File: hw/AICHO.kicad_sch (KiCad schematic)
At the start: 73 parts, among them J1 Conn_01x06, J101 Conn_01x03, J102 Conn_01x02, J103 Conn_01x02, J104 Conn_01x02, J2 Conn_01x02, J201 Conn_01x03, J202 Conn_01x02, J203 Conn_01x02, J204 Conn_01x02, J3 USB_A, J301 Conn_01x03, J302 Conn_01x02, J303 Conn_01x02, J304 Conn_01x02, J4 AudioJack3_SwitchTR, J401 Conn_01x03, J402 Conn_01x02, J403 Conn_01x02, J404 Conn_01x02, J5 Speaker, Q1 Si2302, Q10 Si2302, Q11 Si2302, Q12 Si2302, Q2 Si2302, Q3 Si2302, Q4 Si2302, Q5 Si2302, Q6 Si2302, Q7 Si2302, Q8 Si2302, Q9 Si2302, U1 RP2040, U2 W25Q128JVPIQ, U3 SPX3819M5-L-3-3, U4 USBLC6-2SC6, U5 MAX98357AETE+, Y1 12MHz

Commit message: More routing (is this perfectionism??)
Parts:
- added C17: 100n, Capacitor_SMD:C_0402_1005Metric, symbol Device:C
- added J22: Conn_01x02, Connector_PinHeader_2.54mm:PinHeader_1x02_P2.54mm_Vertical, symbol Connector_Generic:Conn_01x02
- renumbered C17 to C18, C18 to C19, J2 to J21
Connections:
- net +5V: now also C17.1, J22.1 (Pin_1)
- net GND: now also C17.2, J22.2 (Pin_2)
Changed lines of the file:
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@@
   (junction (at 159.385 29.845) (diameter 0) (color 0 0 0 0)
   )
+  (junction (at 252.095 34.29) (diameter 0) (color 0 0 0 0)
+  )
   (junction (at 31.115 26.035) (diameter 0) (color 0 0 0 0)
   )
@@
     (stroke (width 0) (type default))
   )
+  (wire (pts (xy 47.625 26.035) (xy 45.72 26.035))
+    (stroke (width 0) (type default))
+  )
   (wire (pts (xy 262.89 140.97) (xy 264.795 140.97))
     (stroke (width 0) (type default))
@@
     (stroke (width 0) (type default))
   )
+  (wire (pts (xy 47.625 28.575) (xy 45.72 28.575))
+    (stroke (width 0) (type default))
+  )
   (wire (pts (xy 142.24 207.01) (xy 143.51 207.01))
     (stroke (width 0) (type default))
@@
     (stroke (width 0) (type default))
   )
+  (wire (pts (xy 252.095 34.29) (xy 252.095 43.18))
+    (stroke (width 0) (type default))
+  )
   (wire (pts (xy 158.115 81.28) (xy 156.21 81.28))
     (stroke (width 0) (type default))
@@
     (stroke (width 0) (type default))
   )
+  (wire (pts (xy 252.095 34.29) (xy 258.445 34.29))
+    (stroke (width 0) (type default))
+  )
   (wire (pts (xy 101.6 154.94) (xy 102.87 154.94))
     (stroke (width 0) (type default))
@@
   (symbol (lib_id "Connector_Generic:Conn_01x02") (at 24.13 26.035 0) (mirror y) (unit 1)
     (in_bom yes) (on_board yes) (dnp no)
-    (property "Reference" "J2" (at 24.13 22.86 0)
+    (property "Reference" "J21" (at 24.13 22.86 0)
       (effects (font (size 1.27 1.27)))
     )
@@
       (project "AICHO"
         (path "/1352642d-7cf1-4ee5-b8a3-66f2011ace6c"
-          (reference "J2") (unit 1)
+          (reference "J21") (unit 1)
         )
       )
@@
     )
   )
+  (symbol (lib_id "power:GND") (at 258.445 41.91 0) (mirror y) (unit 1)
+    (in_bom yes) (on_board yes) (dnp no)
+    (property "Reference" "#PWR069" (at 258.445 48.26 0)
+      (effects (font (size 1.27 1.27)) hide)
+    )
+    (property "Value" "GND" (at 258.445 46.355 0)
+      (effects (font (size 1.27 1.27)) hide)
+    )
+    (property "Footprint" "" (at 258.445 41.91 0)
+      (effects (font (size 1.27 1.27)) hide)
+    )
+    (property "Datasheet" "" (at 258.445 41.91 0)
+      (effects (font (size 1.27 1.27)) hide)
+    )
+    (pin "1")
+    (instances
+      (project "AICHO"
+        (path "/1352642d-7cf1-4ee5-b8a3-66f2011ace6c"
+          (reference "#PWR069") (unit 1)
+        )
+      )
+    )
+  )
   (symbol (lib_id "power:+5V") (at 151.13 197.485 0) (unit 1)
     (in_bom yes) (on_board yes) (dnp no) (fields_autoplaced)
@@
     )
   )
+  (symbol (lib_id "Connector_Generic:Conn_01x02") (at 40.64 26.035 0) (mirror y) (unit 1)
+    (in_bom yes) (on_board yes) (dnp no)
+    (property "Reference" "J22" (at 40.64 22.86 0)
+      (effects (font (size 1.27 1.27)))
+    )
+    (property "Value" "Conn_01x02" (at 40.64 22.86 0)
+      (effects (font (size 1.27 1.27)) hide)
+    )
+    (property "Footprint" "Connector_PinHeader_2.54mm:PinHeader_1x02_P2.54mm_Vertical" (at 40.64 26.035 0)
+      (effects (font (size 1.27 1.27)) hide)
+    )
+    (property "Datasheet" "~" (at 40.64 26.035 0)
+      (effects (font (size 1.27 1.27)) hide)
+    )
+    (pin "2")
+    (pin "1")
+    (instances
+      (project "AICHO"
+        (path "/1352642d-7cf1-4ee5-b8a3-66f2011ace6c"
+          (reference "J22") (unit 1)
+        )
+      )
+    )
+  )
   (symbol (lib_id "Regulator_Linear:SPX3819M5-L-3-3") (at 38.1 44.45 0) (unit 1)
     (in_bom yes) (on_board yes) (dnp no) (fields_autoplaced)
@@
     )
   )
-  (symbol (lib_id "power:+5V") (at 252.095 43.18 0) (unit 1)
+  (symbol (lib_id "power:+5V") (at 252.095 34.29 0) (unit 1)
     (in_bom yes) (on_board yes) (dnp no) (fields_autoplaced)
-    (property "Reference" "#PWR024" (at 252.095 46.99 0)
+    (property "Reference" "#PWR024" (at 252.095 38.1 0)
       (effects (font (size 1.27 1.27)) hide)
     )
-    (property "Value" "+5V" (at 252.095 38.735 0)
+    (property "Value" "+5V" (at 252.095 29.845 0)
       (effects (font (size 1.27 1.27)))
     )
-    (property "Footprint" "" (at 252.095 43.18 0)
+    (property "Footprint" "" (at 252.095 34.29 0)
       (effects (font (size 1.27 1.27)) hide)
     )
-    (property "Datasheet" "" (at 252.095 43.18 0)
+    (property "Datasheet" "" (at 252.095 34.29 0)
       (effects (font (size 1.27 1.27)) hide)
     )
@@
   )
   (symbol (lib_id "Power_Protection:USBLC6-2SC6") (at 252.095 53.34 0) (unit 1)
-    (in_bom yes) (on_board yes) (dnp no) (fields_autoplaced)
-    (property "Reference" "U4" (at 253.7461 40.64 0)
+    (in_bom yes) (on_board yes) (dnp no)
+    (property "Reference" "U4" (at 255.27 62.865 0)
       (effects (font (size 1.27 1.27)) (justify left))
     )
-    (property "Value" "USBLC6-2SC6" (at 253.7461 43.18 0)
+    (property "Value" "USBLC6-2SC6" (at 255.27 65.405 0)
       (effects (font (size 1.27 1.27)) (justify left))
     )
@@
   (symbol (lib_id "Device:C") (at 235.585 127 0) (unit 1)
     (in_bom yes) (on_board yes) (dnp no)
-    (property "Reference" "C18" (at 238.76 125.73 0)
+    (property "Reference" "C19" (at 238.76 125.73 0)
       (effects (font (size 1.27 1.27)) (justify left))
     )
@@
       (project "AICHO"
         (path "/1352642d-7cf1-4ee5-b8a3-66f2011ace6c"
-          (reference "C18") (unit 1)
+          (reference "C19") (unit 1)
         )
       )
@@
   (symbol (lib_id "Device:C") (at 224.155 127 0) (unit 1)
     (in_bom yes) (on_board yes) (dnp no)
-    (property "Reference" "C17" (at 227.33 125.73 0)
+    (property "Reference" "C18" (at 227.33 125.73 0)
       (effects (font (size 1.27 1.27)) (justify left))
     )
@@
       (project "AICHO"
         (path "/1352642d-7cf1-4ee5-b8a3-66f2011ace6c"
-          (reference "C17") (unit 1)
+          (reference "C18") (unit 1)
         )
       )
@@
     )
   )
+  (symbol (lib_id "Device:C") (at 258.445 38.1 0) (unit 1)
+    (in_bom yes) (on_board yes) (dnp no)
+    (property "Reference" "C17" (at 261.62 36.83 0)
+      (effects (font (size 1.27 1.27)) (justify left))
+    )
+    (property "Value" "100n" (at 261.62 39.37 0)
+      (effects (font (size 1.27 1.27)) (justify left))
+    )
+    (property "Footprint" "Capacitor_SMD:C_0402_1005Metric" (at 259.4102 41.91 0)
+      (effects (font (size 1.27 1.27)) hide)
+    )
+    (property "Datasheet" "~" (at 258.445 38.1 0)
+      (effects (font (size 1.27 1.27)) hide)
+    )
+    (pin "2")
+    (pin "1")
+    (instances
+      (project "AICHO"
+        (path "/1352642d-7cf1-4ee5-b8a3-66f2011ace6c"
+          (reference "C17") (unit 1)
+        )
+      )
+    )
+  )
   (symbol (lib_id "power:GND") (at 151.13 186.055 0) (unit 1)
     (in_bom yes) (on_board yes) (dnp no) (fields_autoplaced)
@@
     )
   )
+  (symbol (lib_id "power:GND") (at 47.625 28.575 0) (unit 1)
+    (in_bom yes) (on_board yes) (dnp no) (fields_autoplaced)
+    (property "Reference" "#PWR071" (at 47.625 34.925 0)
+      (effects (font (size 1.27 1.27)) hide)
+    )
+    (property "Value" "GND" (at 47.625 33.02 0)
+      (effects (font (size 1.27 1.27)) hide)
+    )
+    (property "Footprint" "" (at 47.625 28.575 0)
+      (effects (font (size 1.27 1.27)) hide)
+    )
+    (property "Datasheet" "" (at 47.625 28.575 0)
+      (effects (font (size 1.27 1.27)) hide)
+    )
+    (pin "1")
+    (instances
+      (project "AICHO"
+        (path "/1352642d-7cf1-4ee5-b8a3-66f2011ace6c"
+          (reference "#PWR071") (unit 1)
+        )
+      )
+    )
+  )
   (symbol (lib_id "power:+5V") (at 110.49 145.415 0) (unit 1)
     (in_bom yes) (on_board yes) (dnp no) (fields_autoplaced)
@@
         )
       )
+    )
+  )
+  (symbol (lib_id "power:+5V") (at 47.625 26.035 0) (unit 1)
+    (in_bom yes) (on_board yes) (dnp no) (fields_autoplaced)
+    (property "Reference" "#PWR070" (at 47.625 29.845 0)
+      (effects (font (size 1.27 1.27)) hide)
+    )
+    (property "Value" "+5V" (at 47.625 21.59 0)
+      (effects (font (size 1.27 1.27)))
+    )
+    (property "Footprint" "" (at 47.625 26.035 0)
+      (effects (font (size 1.27 1.27)) hide)
+    )
+    (property "Datasheet" "" (at 47.625 26.035 0)
+      (effects (font (size 1.27 1.27)) hide)
+    )
+    (pin "1")
+    (instances
+      (project "AICHO"
+        (path "/1352642d-7cf1-4ee5-b8a3-66f2011ace6c"
+          (reference "#PWR070") (unit 1)
+        )
+      )

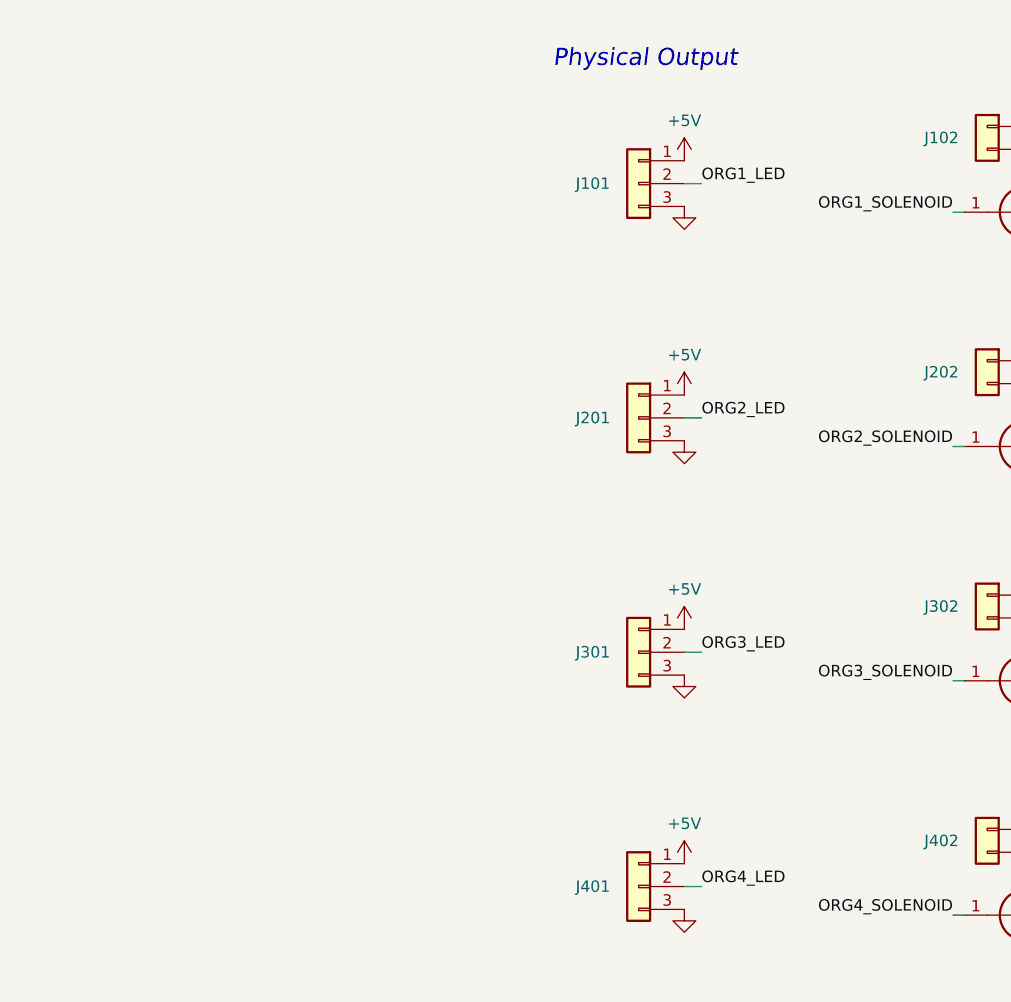
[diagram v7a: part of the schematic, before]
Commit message: Fix missing level shifter and resubmit for fab >-<
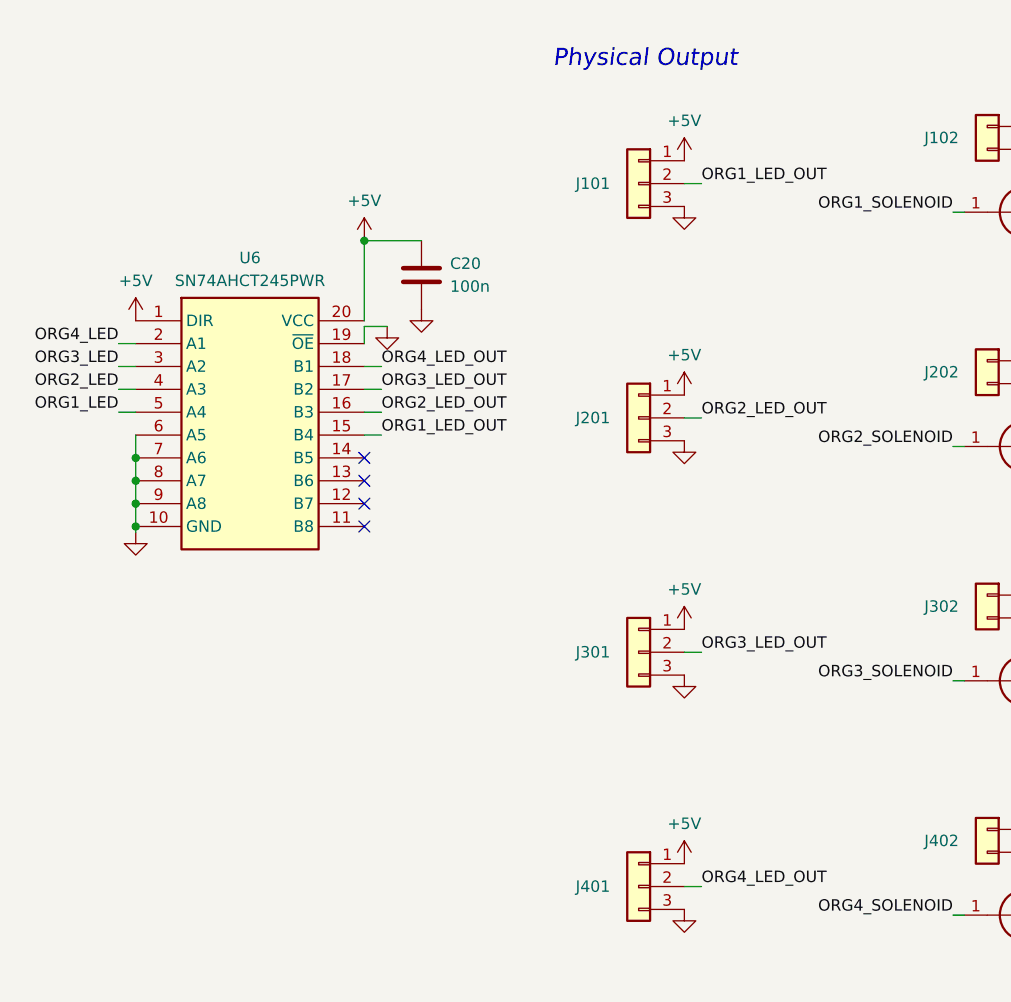
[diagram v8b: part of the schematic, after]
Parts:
- added C20: 100n, Capacitor_SMD:C_0402_1005Metric, symbol Device:C
- added U6: SN74AHCT245PWR, SN74AHCT245PWR:SOP65P640X120-20N, symbol SN74AHCT245PWR:SN74AHCT245PWR
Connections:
- net +5V: now also C20.1, U6.1 (DIR), U6.20 (VCC)
- net GND: now also C20.2, U6.10 (GND), U6.19 (~{OE}), U6.6 (A5), U6.7 (A6), U6.8 (A7), U6.9 (A8)
- net ORG1_LED: now also U6.5 (A4); no longer J101.2 (Pin_2)
- net ORG2_LED: now also U6.4 (A3); no longer J201.2 (Pin_2)
- net ORG3_LED: now also U6.3 (A2); no longer J301.2 (Pin_2)
- net ORG4_LED: now also U6.2 (A1); no longer J401.2 (Pin_2)
- new net ORG1_LED_OUT: J101.2 (Pin_2), U6.15 (B4)
- new net ORG2_LED_OUT: J201.2 (Pin_2), U6.16 (B3)
- new net ORG3_LED_OUT: J301.2 (Pin_2), U6.17 (B2)
- new net ORG4_LED_OUT: J401.2 (Pin_2), U6.18 (B1)
- no-connect marks 12 -> 16
